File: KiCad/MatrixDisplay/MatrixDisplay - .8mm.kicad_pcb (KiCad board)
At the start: 2 copper layers, 3 parts, among them J1 PUT_IN, J2 Power, U1 mini_esp32

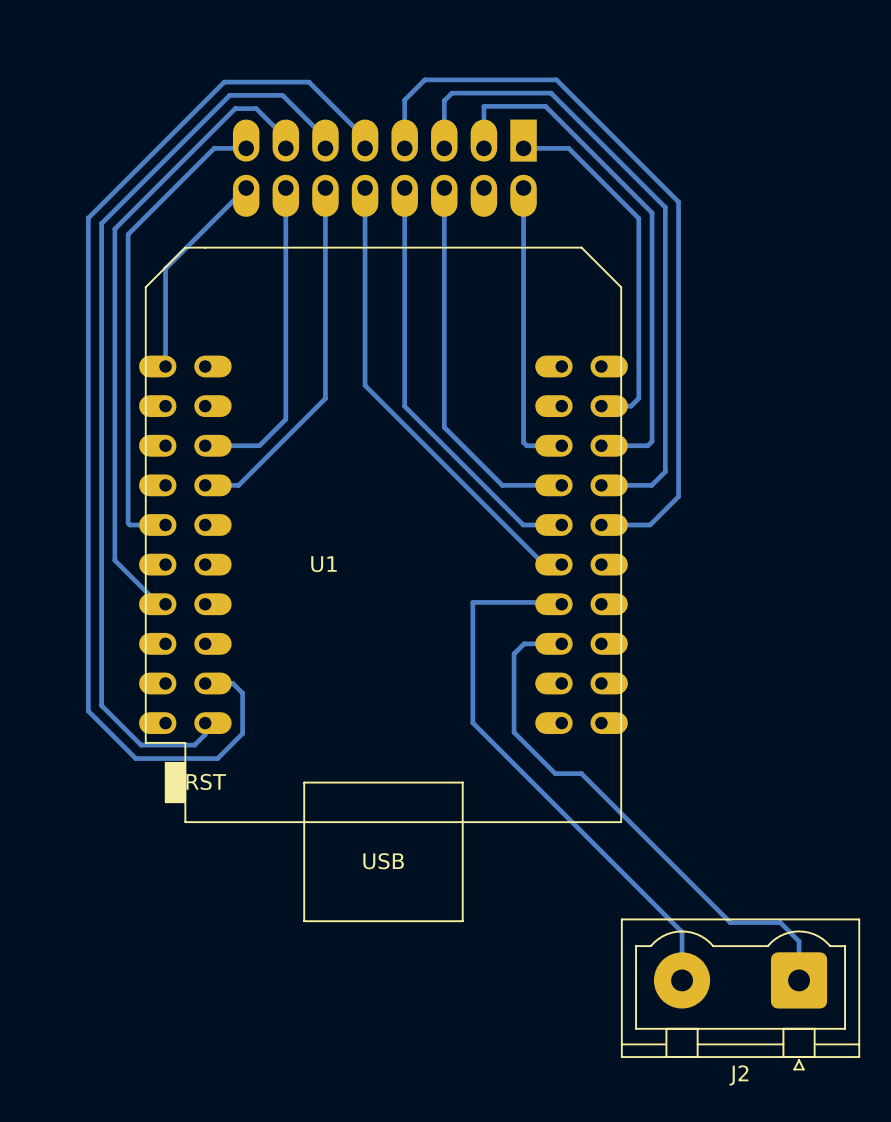
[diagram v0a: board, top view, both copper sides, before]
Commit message: add wifi setup instructins to display
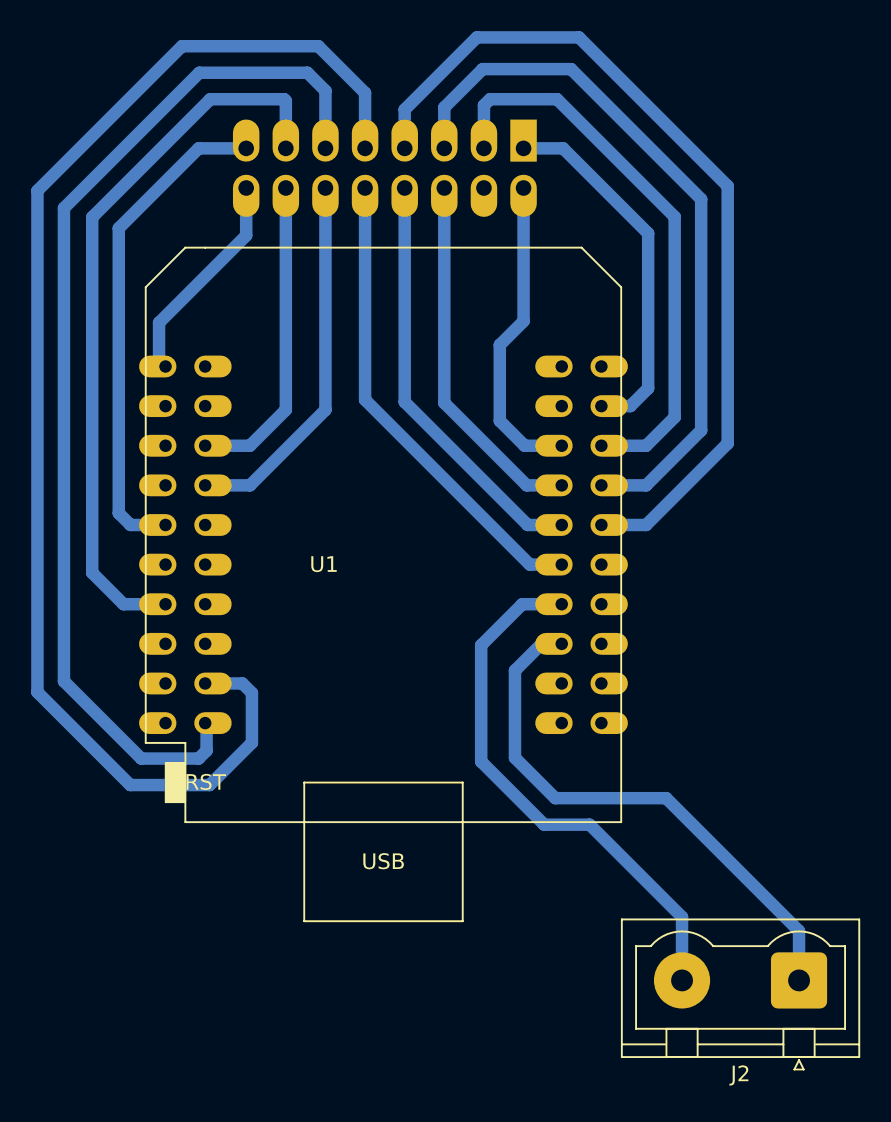
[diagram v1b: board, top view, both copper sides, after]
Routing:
- net Net-(U1-Pad18): track 72.2 -> 85.6 mm
- net Net-(U1-Pad20): track 59.2 -> 68.6 mm
- net Net-(J1-Pad7): track 49.0 -> 55.8 mm
- net Net-(U1-Pad13): track 41.3 -> 47.0 mm
- net Net-(J1-Pad5): track 41.9 -> 46.2 mm
- net Net-(J1-Pad3): track 34.3 -> 36.6 mm
- net Net-(J1-Pad2): track 18.8 -> 20.2 mm
- net Net-(U1-Pad9): track 30.8 -> 31.9 mm
- net Net-(J1-Pad6): track 24.4 -> 23.5 mm
- net Net-(J2-Pad1): track 34.7 -> 35.3 mm
- net Net-(J1-Pad10): track 30.0 -> 30.6 mm
